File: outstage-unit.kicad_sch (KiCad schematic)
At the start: 10 parts, among them J34001 Conn_01x06_Socket, M34001 Fan

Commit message: edit pss symbol library: export all schematic symbols to library 'pss' and update symbol link
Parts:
- J34001: symbol Connector:Conn_01x06_Socket -> pss:Conn_01x06_Socket
- JP34001: symbol Jumper:SolderJumper_2_Bridged -> pss:SolderJumper_2_Bridged
- TP34001, TP34002, TP34003, TP34004, TP34005, TP34006: symbol Connector:TestPoint -> pss:TestPoint
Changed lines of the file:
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@@
 	)
 	(symbol
-		(lib_id "Jumper:SolderJumper_2_Bridged")
+		(lib_id "pss:SolderJumper_2_Bridged")
 		(at 157.48 167.64 270)
 		(unit 1)
@@
 	)
 	(symbol
-		(lib_id "Connector:TestPoint")
+		(lib_id "pss:TestPoint")
 		(at 77.47 176.53 0)
 		(unit 1)
@@
 	)
 	(symbol
-		(lib_id "Connector:TestPoint")
+		(lib_id "pss:TestPoint")
 		(at 74.93 173.99 0)
 		(unit 1)
@@
 	)
 	(symbol
-		(lib_id "Connector:TestPoint")
+		(lib_id "pss:TestPoint")
 		(at 80.01 179.07 0)
 		(unit 1)
@@
 	)
 	(symbol
-		(lib_id "Connector:TestPoint")
+		(lib_id "pss:TestPoint")
 		(at 85.09 184.15 0)
 		(unit 1)
@@
 	)
 	(symbol
-		(lib_id "Connector:Conn_01x06_Socket")
+		(lib_id "pss:Conn_01x06_Socket")
 		(at 48.26 176.53 0)
 		(mirror y)
@@
 	)
 	(symbol
-		(lib_id "Connector:TestPoint")
+		(lib_id "pss:TestPoint")
 		(at 82.55 181.61 0)
 		(unit 1)
@@
 	)
 	(symbol
-		(lib_id "Connector:TestPoint")
+		(lib_id "pss:TestPoint")
 		(at 72.39 171.45 0)
 		(unit 1)

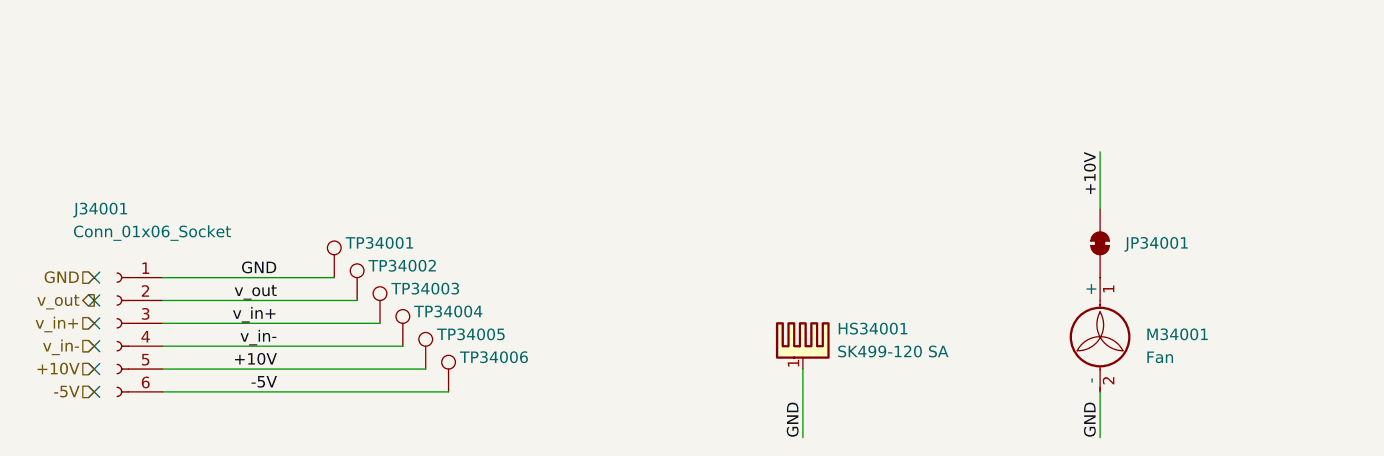
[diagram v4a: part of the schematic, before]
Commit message: edit pss footprint library: export all footprints to library 'pss' and update footprint links
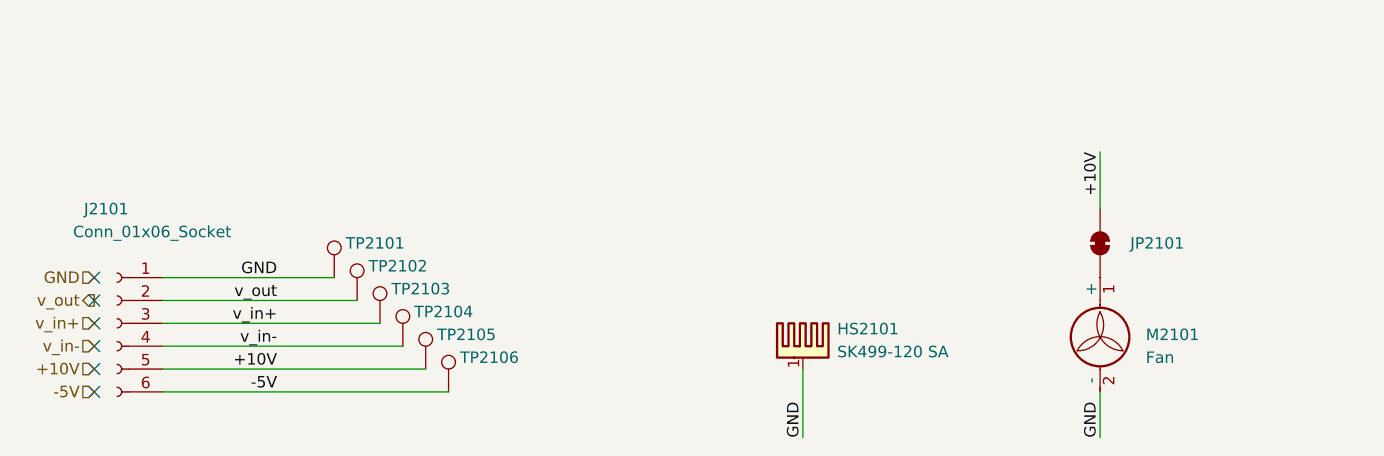
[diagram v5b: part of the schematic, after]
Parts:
- renumbered HS34001 to HS2101, J34001 to J2101, JP34001 to JP2101, M34001 to M2101, TP34001 to TP2101, TP34002 to TP2102, TP34003 to TP2103, TP34004 to TP2104, TP34005 to TP2105, TP34006 to TP2106
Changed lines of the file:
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@@
 		(dnp no)
 		(fields_autoplaced yes)
-		(property "Reference" "HS34001"
+		(property "Reference" "HS2101"
 			(at 128.27 177.1649 0)
 			(effects
@@
 		(on_board yes)
 		(dnp no)
-		(property "Reference" "JP34001"
+		(property "Reference" "JP2101"
 			(at 163.83 167.64 90)
 			(effects
@@
 		(on_board yes)
 		(dnp no)
-		(property "Reference" "TP34003"
+		(property "Reference" "TP2103"
 			(at 78.74 172.72 0)
 			(effects
@@
 		(on_board yes)
 		(dnp no)
-		(property "Reference" "TP34002"
+		(property "Reference" "TP2102"
 			(at 76.2 170.18 0)
 			(effects
@@
 		(on_board yes)
 		(dnp no)
-		(property "Reference" "TP34004"
+		(property "Reference" "TP2104"
 			(at 81.28 175.26 0)
 			(effects
@@
 		(on_board yes)
 		(dnp no)
-		(property "Reference" "TP34006"
+		(property "Reference" "TP2106"
 			(at 86.36 180.34 0)
 			(effects
@@
 		(on_board yes)
 		(dnp no)
-		(property "Reference" "J34001"
+		(property "Reference" "J2101"
 			(at 49.53 163.83 0)
 			(effects
@@
 		(dnp no)
 		(fields_autoplaced yes)
-		(property "Reference" "M34001"
+		(property "Reference" "M2101"
 			(at 162.56 177.7999 0)
 			(effects
@@
 		(on_board yes)
 		(dnp no)
-		(property "Reference" "TP34005"
+		(property "Reference" "TP2105"
 			(at 83.82 177.8 0)
 			(effects
@@
 		(on_board yes)
 		(dnp no)
-		(property "Reference" "TP34001"
+		(property "Reference" "TP2101"
 			(at 73.66 167.64 0)
 			(effects
